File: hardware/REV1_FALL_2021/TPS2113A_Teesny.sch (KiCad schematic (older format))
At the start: 6 parts, among them U201 TPS2113ADRBR

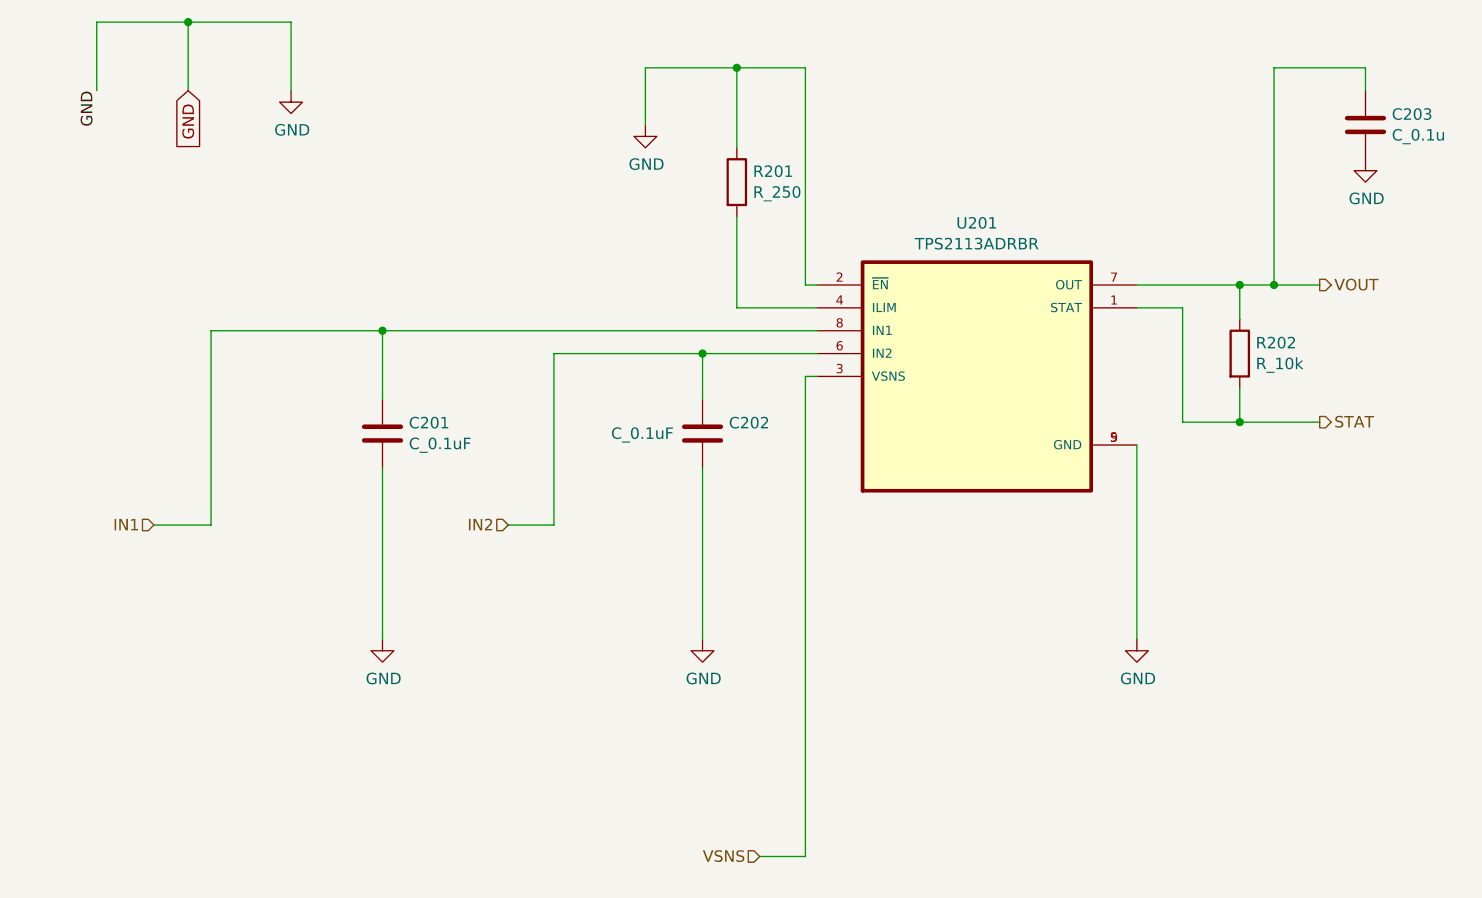
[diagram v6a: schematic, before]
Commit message: change resistance of one voltage divider resistor
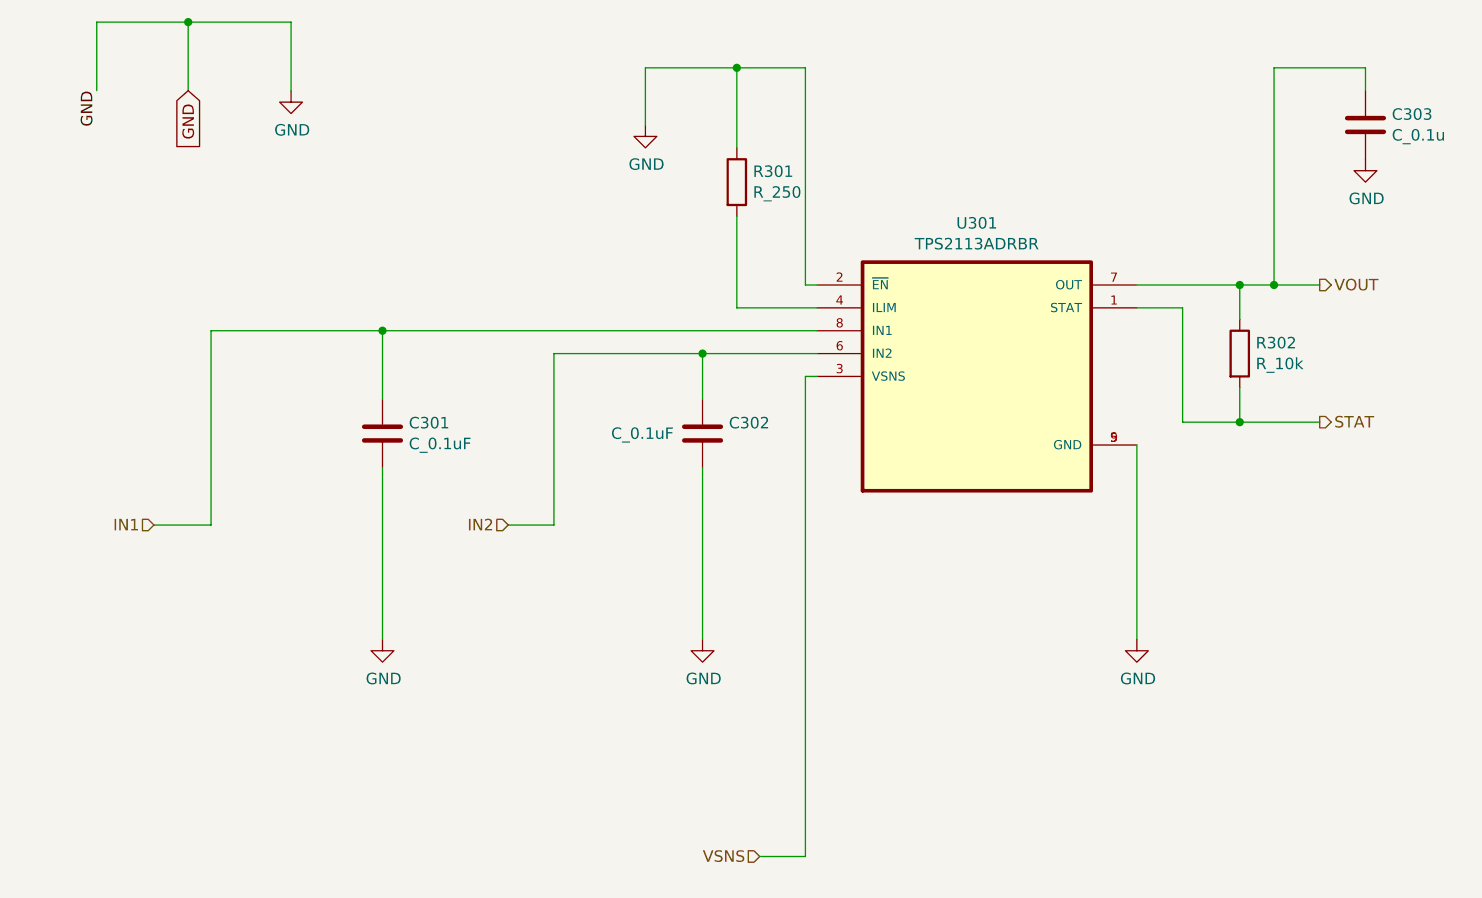
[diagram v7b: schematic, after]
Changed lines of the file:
@@
 $Descr A4 11693 8268
 encoding utf-8
-Sheet 2 3
+Sheet 3 3
 Title ""
 Date ""
@@
 AR Path="/61A02CEE/61AB462E" Ref="U201"  Part="1"
 AR Path="/619AC3BC/61AB462E" Ref="U301"  Part="1"
-F 0 "U201" H 6600 3720 50  0000 C CNN
+F 0 "U301" H 6600 3720 50  0000 C CNN
 F 1 "TPS2113ADRBR" H 6600 3629 50  0000 C CNN
 F 2 "footprints:TPS2113ADRBR" H 6600 3050 50  0001 L BNN
@@
 AR Path="/619AC3BC/61AB4644" Ref="C301"  Part="1"
 AR Path="/61A02CEE/61AB4644" Ref="C201"  Part="1"
-F 0 "C201" H 4115 3346 50  0000 L CNN
+F 0 "C301" H 4115 3346 50  0000 L CNN
 F 1 "C_0.1uF" H 4115 3255 50  0000 L CNN
 F 2 "Capacitor_SMD:C_0805_2012Metric_Pad1.18x1.45mm_HandSolder" H 4038 3150 50  0001 C CNN
@@
 AR Path="/619AC3BC/61AB464C" Ref="C302"  Part="1"
 AR Path="/61A02CEE/61AB464C" Ref="C202"  Part="1"
-F 0 "C202" H 5515 3346 50  0000 L CNN
+F 0 "C302" H 5515 3346 50  0000 L CNN
 F 1 "C_0.1uF" H 5000 3300 50  0000 L CNN
 F 2 "Capacitor_SMD:C_0805_2012Metric_Pad1.18x1.45mm_HandSolder" H 5438 3150 50  0001 C CNN
@@
 AR Path="/619AC3BC/61AB465E" Ref="R301"  Part="1"
 AR Path="/61A02CEE/61AB465E" Ref="R201"  Part="1"
-F 0 "R201" H 5620 2246 50  0000 L CNN
+F 0 "R301" H 5620 2246 50  0000 L CNN
 F 1 "R_250" H 5620 2155 50  0000 L CNN
 F 2 "Resistor_SMD:R_0805_2012Metric_Pad1.20x1.40mm_HandSolder" V 5480 2200 50  0001 C CNN
@@
 AR Path="/619AC3BC/61AB4669" Ref="#PWR0113"  Part="1"
 AR Path="/61A02CEE/61AB4669" Ref="#PWR0121"  Part="1"
-F 0 "#PWR0121" H 5150 1700 50  0001 C CNN
+F 0 "#PWR0113" H 5150 1700 50  0001 C CNN
 F 1 "GND" H 5155 1777 50  0000 C CNN
 F 2 "" H 5150 1950 50  0001 C CNN
@@
 AR Path="/619AC3BC/61AB4675" Ref="#PWR0115"  Part="1"
 AR Path="/61A02CEE/61AB4675" Ref="#PWR0123"  Part="1"
-F 0 "#PWR0123" H 4000 3950 50  0001 C CNN
+F 0 "#PWR0115" H 4000 3950 50  0001 C CNN
 F 1 "GND" H 4005 4027 50  0000 C CNN
 F 2 "" H 4000 4200 50  0001 C CNN
@@
 AR Path="/619AC3BC/61AB4681" Ref="#PWR0117"  Part="1"
 AR Path="/61A02CEE/61AB4681" Ref="#PWR0125"  Part="1"
-F 0 "#PWR0125" H 5400 3950 50  0001 C CNN
+F 0 "#PWR0117" H 5400 3950 50  0001 C CNN
 F 1 "GND" H 5405 4027 50  0000 C CNN
 F 2 "" H 5400 4200 50  0001 C CNN
@@
 AR Path="/619AC3BC/61AB4687" Ref="#PWR0118"  Part="1"
 AR Path="/61A02CEE/61AB4687" Ref="#PWR0126"  Part="1"
-F 0 "#PWR0126" H 7300 3950 50  0001 C CNN
+F 0 "#PWR0118" H 7300 3950 50  0001 C CNN
 F 1 "GND" H 7305 4027 50  0000 C CNN
 F 2 "" H 7300 4200 50  0001 C CNN
@@
 AR Path="/619AC3BC/61AB46B4" Ref="R302"  Part="1"
 AR Path="/61A02CEE/61AB46B4" Ref="R202"  Part="1"
-F 0 "R202" H 7820 2996 50  0000 L CNN
+F 0 "R302" H 7820 2996 50  0000 L CNN
 F 1 "R_10k" H 7820 2905 50  0000 L CNN
 F 2 "Resistor_SMD:R_0805_2012Metric_Pad1.20x1.40mm_HandSolder" V 7680 2950 50  0001 C CNN
@@
 AR Path="/619AC3BC/61AB46C3" Ref="C303"  Part="1"
 AR Path="/61A02CEE/61AB46C3" Ref="C203"  Part="1"
-F 0 "C203" H 8415 1996 50  0000 L CNN
+F 0 "C303" H 8415 1996 50  0000 L CNN
 F 1 "C_0.1u" H 8415 1905 50  0000 L CNN
 F 2 "Capacitor_SMD:C_0805_2012Metric_Pad1.18x1.45mm_HandSolder" H 8338 1800 50  0001 C CNN
@@
 AR Path="/619AC3BC/61AB46CF" Ref="#PWR0119"  Part="1"
 AR Path="/61A02CEE/61AB46CF" Ref="#PWR0127"  Part="1"
-F 0 "#PWR0127" H 8300 1850 50  0001 C CNN
+F 0 "#PWR0119" H 8300 1850 50  0001 C CNN
 F 1 "GND" H 8305 1927 50  0000 C CNN
 F 2 "" H 8300 2100 50  0001 C CNN
@@
 AR Path="/619AC3BC/61ABB0D4" Ref="#PWR0120"  Part="1"
 AR Path="/61A02CEE/61ABB0D4" Ref="#PWR0128"  Part="1"
-F 0 "#PWR0128" H 3600 1550 50  0001 C CNN
+F 0 "#PWR0120" H 3600 1550 50  0001 C CNN
 F 1 "GND" H 3605 1627 50  0000 C CNN
 F 2 "" H 3600 1800 50  0001 C CNN
